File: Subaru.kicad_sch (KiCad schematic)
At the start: 30 parts, among them J1 DB15_Male, J2 SYNC_SEL, J3 USB_C_Power, J4 SYNC_OUT_SEL, J5 Mini-DIN-4-S, J7 DB15_Female_HighDensity, U1 74HC86, U2 BH7236AF, Y1 3.579545M

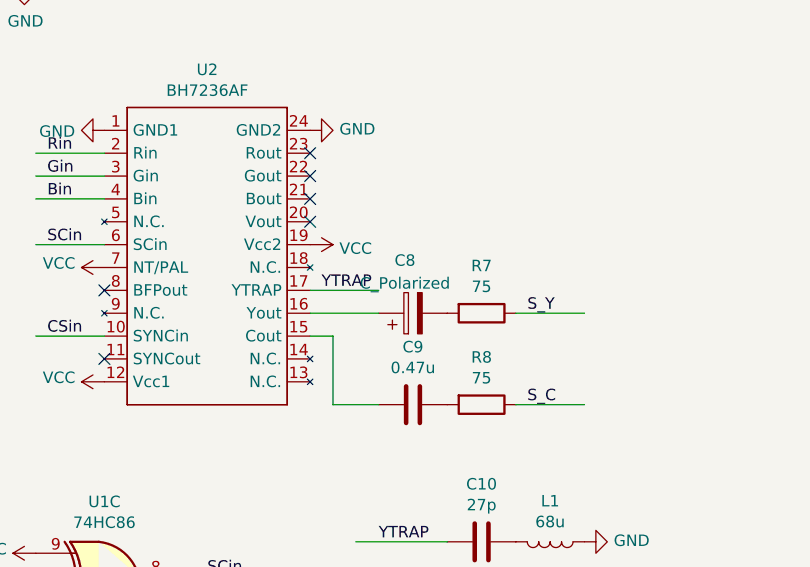
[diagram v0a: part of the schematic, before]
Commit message: update sch to have capacitor's value
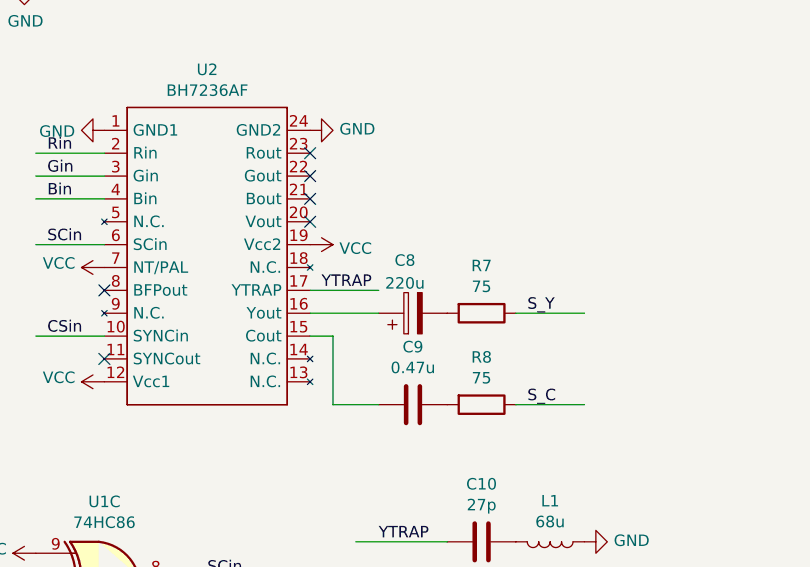
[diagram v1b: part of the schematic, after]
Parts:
- C8: value C_Polarized -> 220u
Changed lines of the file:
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@@
     (in_bom yes) (on_board yes) (fields_autoplaced)
     (property "Reference" "C8" (id 0) (at 165.481 66.5312 90))
-    (property "Value" "C_Polarized" (id 1) (at 165.481 69.0681 90))
+    (property "Value" "220u" (id 1) (at 165.481 69.0681 90))
     (property "Footprint" "Capacitor_THT:CP_Radial_D5.0mm_P2.50mm" (id 2) (at 170.18 71.4248 0)
       (effects (font (size 1.27 1.27)) hide)
@@
     )
     (path "/0fe151f6-fb86-45f5-b30d-1bca1584bc2d"
-      (reference "C8") (unit 1) (value "C_Polarized") (footprint "Capacitor_THT:CP_Radial_D5.0mm_P2.50mm")
+      (reference "C8") (unit 1) (value "220u") (footprint "Capacitor_THT:CP_Radial_D5.0mm_P2.50mm")
     )
     (path "/00000000-0000-0000-0000-00005eaafd00"

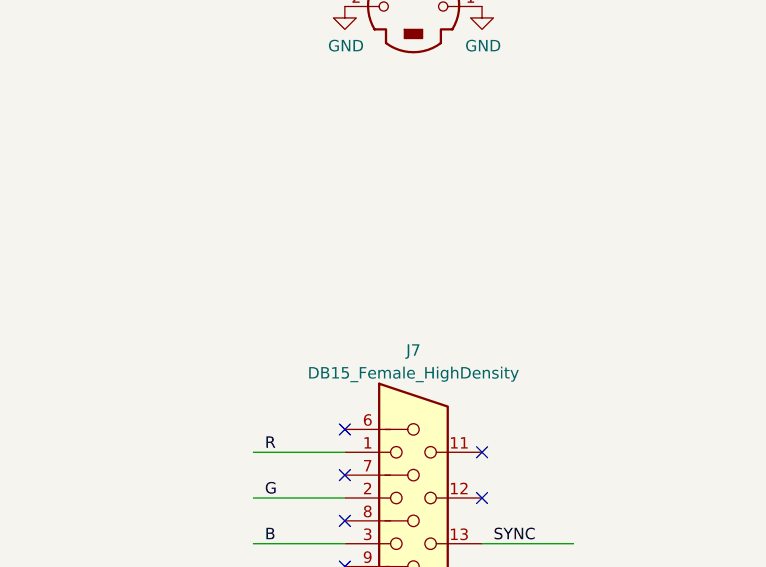
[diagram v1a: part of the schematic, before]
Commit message: feedback from the 1st lot
- modify footprint for S connector
- add a comment on noise in the circuit
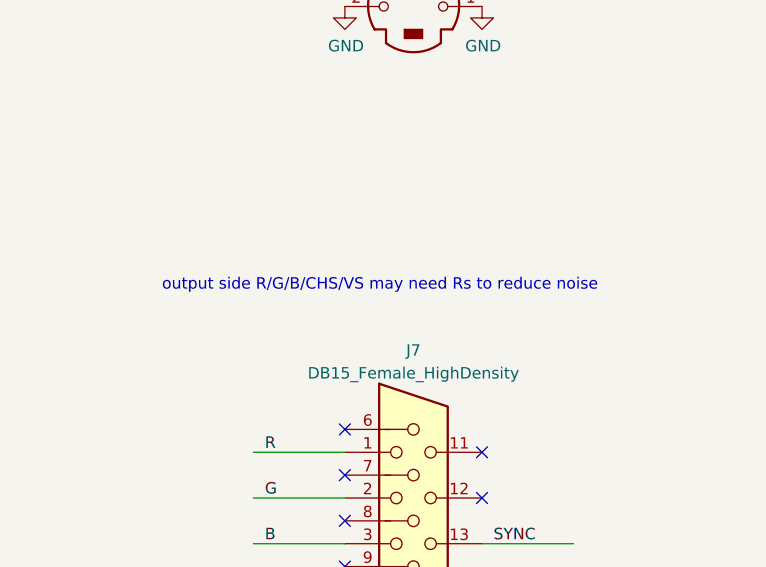
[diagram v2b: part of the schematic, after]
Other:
- note added: "output side R/G/B/CHS/VS may need Rs to reduce noise"
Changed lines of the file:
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@@
+    (effects (font (size 1.27 1.27)) (justify left bottom))
+  )
+  (text "output side R/G/B/CHS/VS may need Rs to reduce noise"
+    (at 213.36 80.01 0)
     (effects (font (size 1.27 1.27)) (justify left bottom))
   )
